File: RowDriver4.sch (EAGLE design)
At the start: 25 parts, among them Q1 DPBT8105, Q2 DPBT8105, Q3 DPBT8105, Q4 DPBT8105

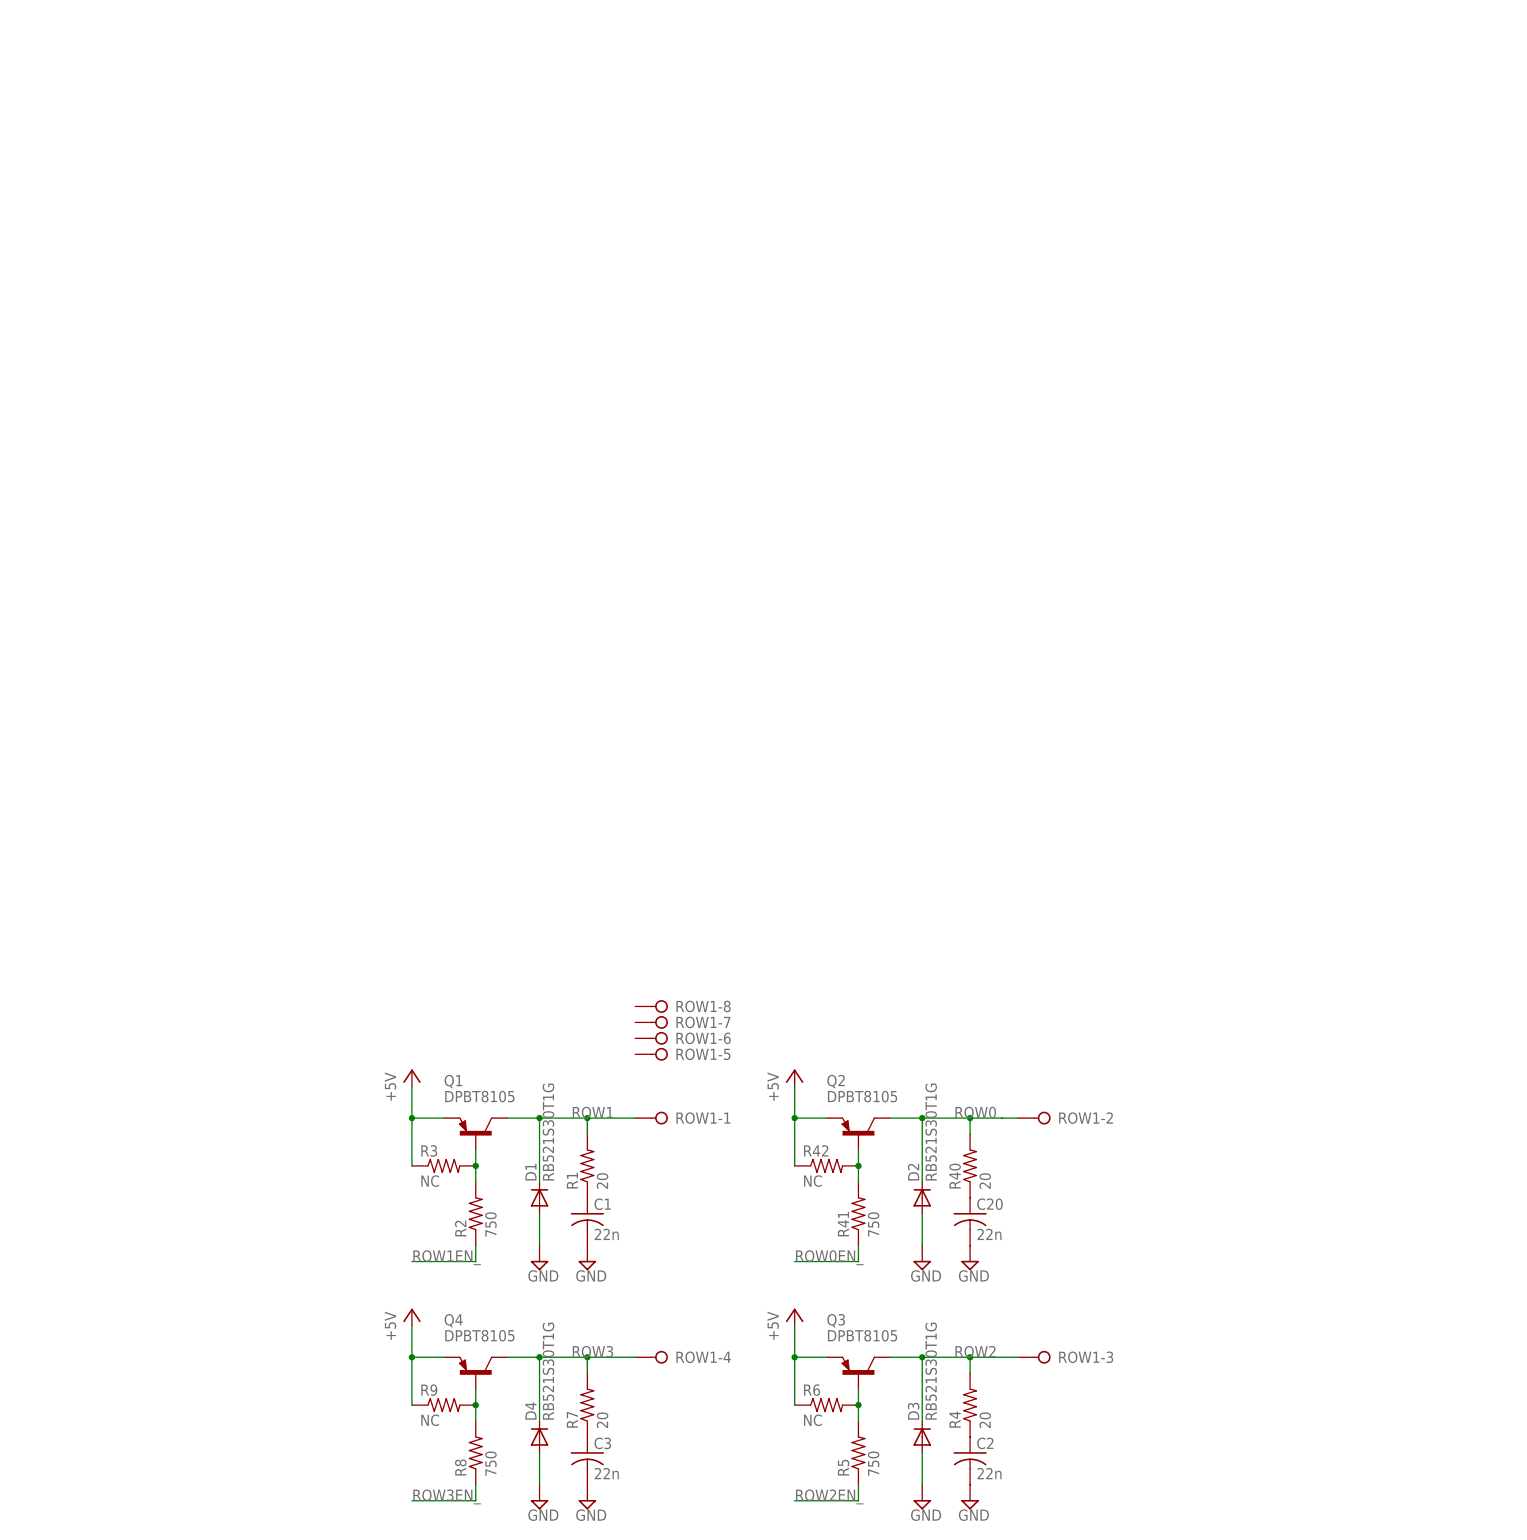
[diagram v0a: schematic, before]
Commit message: Created initial main board. Created layout for row driver, and tiled it. The new board and schematic files for the row driver are intermediate steps.
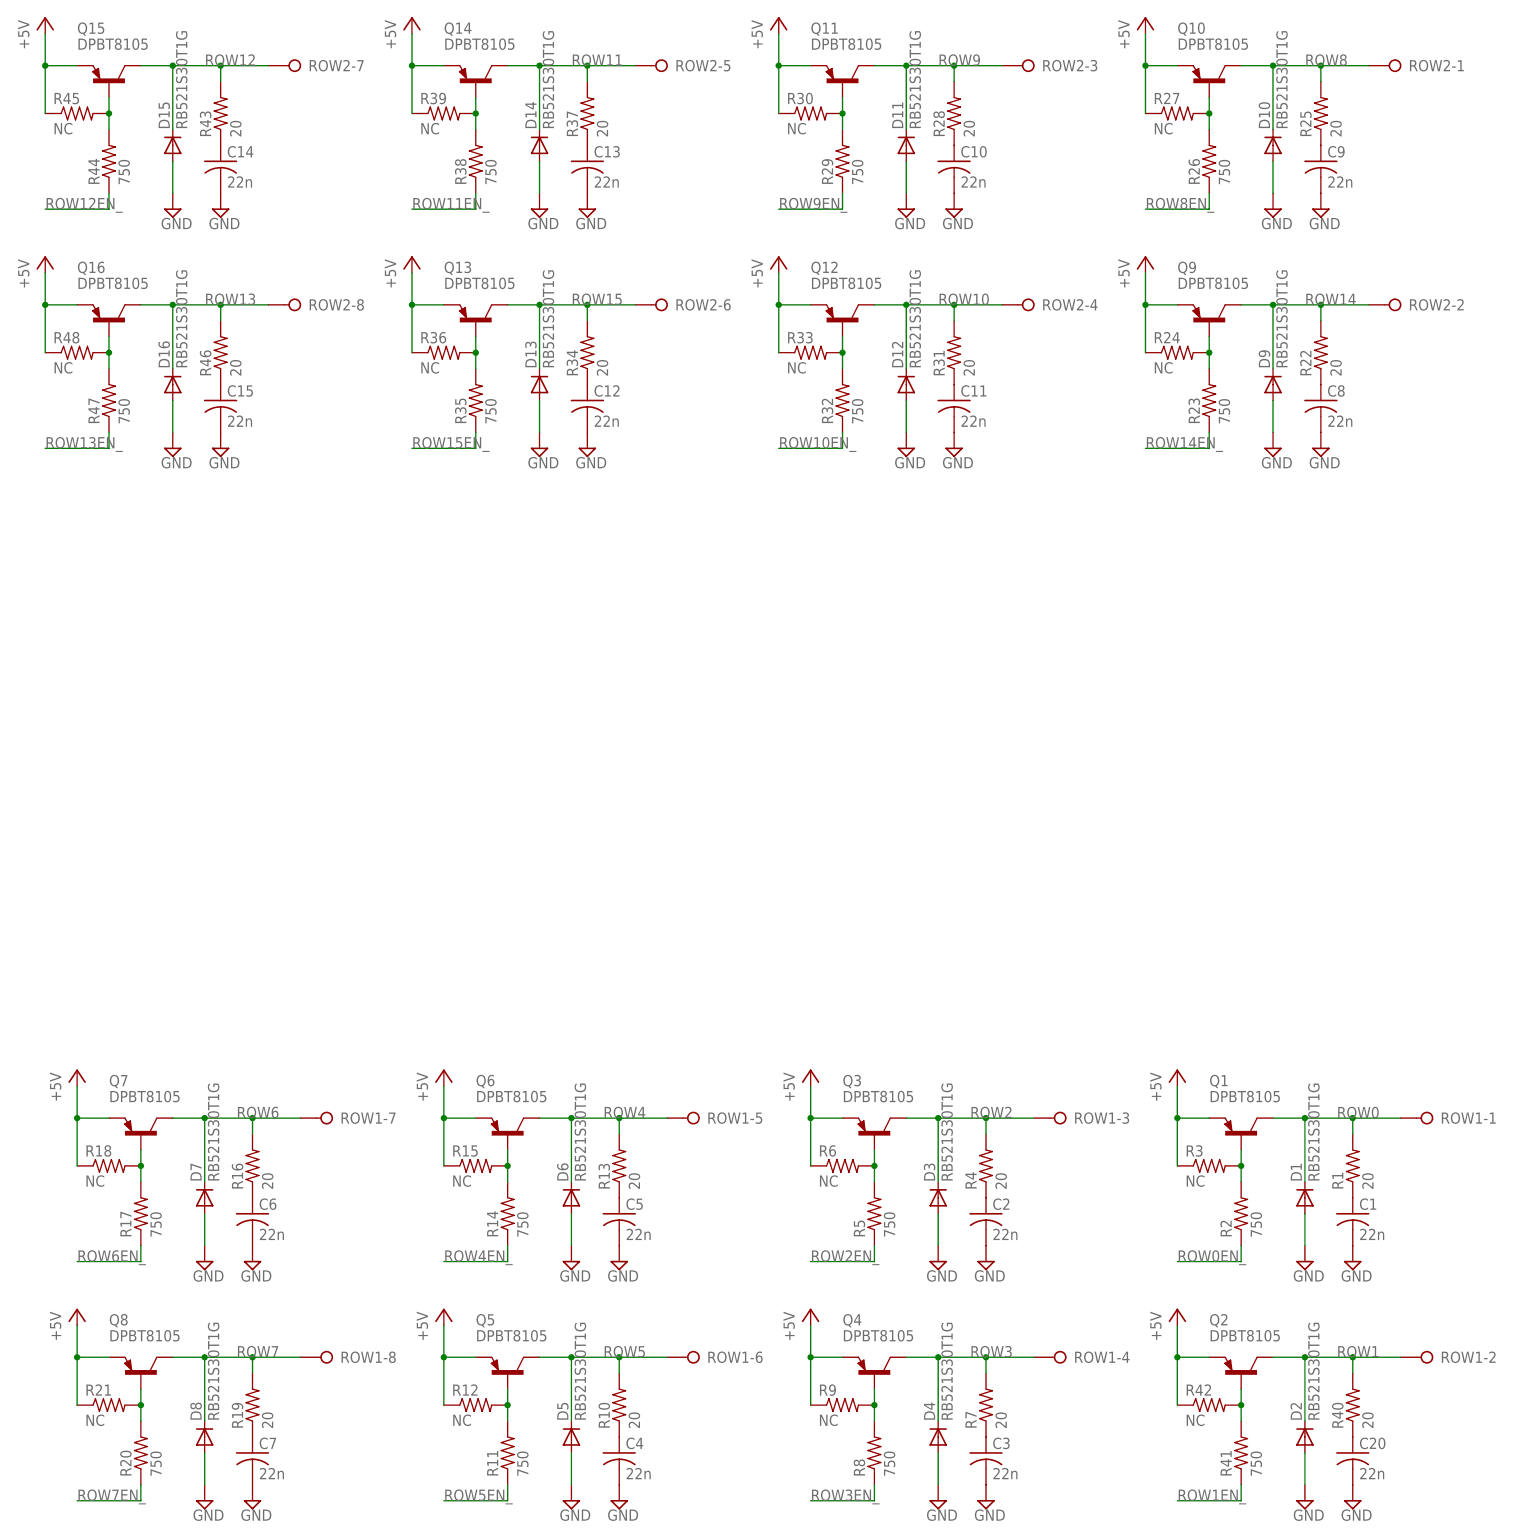
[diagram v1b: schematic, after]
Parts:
- added C10, C11, C12, C13, C14, C15, C4, C5, C6, C7, C8, C9: 22n, resistor:C-USC0603
- added D10, D11, D12, D13, D14, D15, D16, D5, D6, D7, D8, D9: RB521S30T1G, diode:DIODE-SOD523
- added Q10, Q11, Q12, Q13, Q14, Q15, Q16, Q5, Q6, Q7, Q8, Q9: DPBT8105, Parts:DPBT8105
- added R10, R13, R16, R19, R22, R25, R28, R31, R34, R37, R43, R46: 20, resistor:R-US_R0603
- added R11, R14, R17, R20, R23, R26, R29, R32, R35, R38, R44, R47: 750, resistor:R-US_R0603
- added R12, R15, R18, R21, R24, R27, R30, R33, R36, R39, R45, R48: NC, resistor:R-US_R0603
- added ROW2: (no value), Parts:OSTVN08A150
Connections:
- new net N$10: C5.1, R13.1
- new net N$11: Q7.B, R17.2, R18.2
- new net N$12: C6.1, R16.1
- new net N$13: Q8.B, R20.2, R21.2
- new net N$14: C7.1, R19.1
- new net N$15: Q9.B, R23.2, R24.2
- new net N$16: C8.1, R22.1
- new net N$17: Q10.B, R26.2, R27.2
- new net N$18: C9.1, R25.1
- new net N$19: Q11.B, R29.2, R30.2
- new net N$20: C10.1, R28.1
- new net N$21: Q12.B, R32.2, R33.2
- new net N$22: C11.1, R31.1
- new net N$23: Q13.B, R35.2, R36.2
- new net N$24: C12.1, R34.1
- new net N$25: Q14.B, R38.2, R39.2
- new net N$26: C13.1, R37.1
- new net N$27: Q15.B, R44.2, R45.2
- new net N$28: C14.1, R43.1
- new net N$29: Q16.B, R47.2, R48.2
- new net N$30: C15.1, R46.1
- new net N$7: Q5.B, R11.2, R12.2
- new net N$8: C4.1, R10.1
- new net N$9: Q6.B, R14.2, R15.2
- new net ROW10: D12.C, Q12.C, R31.2, ROW2-4.KL
- new net ROW10EN_: R32.1
- new net ROW11: D14.C, Q14.C, R37.2, ROW2-5.KL
- new net ROW11EN_: R38.1
- new net ROW12: D15.C, Q15.C, R43.2, ROW2-7.KL
- new net ROW12EN_: R44.1
- new net ROW13: D16.C, Q16.C, R46.2, ROW2-8.KL
- new net ROW13EN_: R47.1
- new net ROW14: D9.C, Q9.C, R22.2, ROW2-2.KL
- new net ROW14EN_: R23.1
- new net ROW15: D13.C, Q13.C, R34.2, ROW2-6.KL
- new net ROW15EN_: R35.1
- new net ROW4: D6.C, Q6.C, R13.2, ROW1-5.KL
- new net ROW4EN_: R14.1
- new net ROW5: D5.C, Q5.C, R10.2, ROW1-6.KL
- new net ROW5EN_: R11.1
- new net ROW6: D7.C, Q7.C, R16.2, ROW1-7.KL
- new net ROW6EN_: R17.1
- new net ROW7: D8.C, Q8.C, R19.2, ROW1-8.KL
- new net ROW7EN_: R20.1
- new net ROW8: D10.C, Q10.C, R25.2, ROW2-1.KL
- new net ROW8EN_: R26.1
- new net ROW9: D11.C, Q11.C, R28.2, ROW2-3.KL
- new net ROW9EN_: R29.1
- net +5V: now also Q10.E, Q11.E, Q12.E, Q13.E, Q14.E, Q15.E, Q16.E, Q5.E, Q6.E, Q7.E, Q8.E, Q9.E, R12.1, R15.1, R18.1, R21.1, R24.1, R27.1, R30.1, R33.1, R36.1, R39.1, R45.1, R48.1
- net GND: now also C10.2, C11.2, C12.2, C13.2, C14.2, C15.2, C4.2, C5.2, C6.2, C7.2, C8.2, C9.2, D10.A, D11.A, D12.A, D13.A, D14.A, D15.A, D16.A, D5.A, D6.A, D7.A, D8.A, D9.A
- net ROW0: now also D1.C, Q1.C, R1.2, ROW1-1.KL; no longer D2.C, Q2.C, R40.2, ROW1-2.KL
- net ROW0EN_: now also R2.1; no longer R41.1
- net ROW1: now also D2.C, Q2.C, R40.2, ROW1-2.KL; no longer D1.C, Q1.C, R1.2, ROW1-1.KL
- net ROW1EN_: now also R41.1; no longer R2.1
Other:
- moved on the sheet: C1, C2, C20, C3, D1, D2, D3, D4, Q1, Q2, Q3, Q4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

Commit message: Iterated through a few possible board floorplans.  Routing will be incredibly tight, but I thought of a few possibilities that ease those concerns.
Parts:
- added C16, C21, C22, C89, C90, C91, C92, C94, C95, C96, C97, C98: NC, rcl:C-USC0805
- added C17, C18, C19, C26, C27, C28, C29, C31, C33, C93: 0.1uF, rcl:C-USC0805
- added C23: 470pF, rcl:C-USC0805
- added C24, C38: 10uF, rcl:C-USC1206K
- added C25, C30, C32, C36, C39: 1uF, rcl:C-USC0805
- added C34, C35, C37, C40: 100uF, resistor:CPOL-USD
- added C41, C42, C43, C44, C45, C46, C47, C48, C49, C50, C51, C52, C53, C54, C55, C56, C57, C58, C59, C60, C61, C62, C63, C64, C65, C66, C67, C68, C69, C70, C71, C72, C73, C74, C75, C76, C77, C78, C79, C80, C81, C82, C83, C84, C85, C86, C87, C88: 1n, resistor:C-USC0805
- added D17, D18, D19, D20, D21, D22, D23, D24, D25, D26, D27, D28, D29, D30, D31, D32, D33, D34, D35, D36, D37, D38, D39, D40, D41, D42, D43, D44, D45, D46, D47, D48, D49, D50, D51, D52, D53, D54, D55, D56, D57, D58, D59, D60, D61, D62, D63, D64: RB521S30T1G, diode:DIODE-SOD523
- added IC1, IC2: 74HCT138D, Parts:74HCT138D
- added IC3: PIC24FJ32GB004, Parts:PIC24FJ32GB004
- added IC4, IC5: SN74LV4052AD, Parts:SN74LV4052AD
- added IC6: TC1015, Parts:TC1015
- added IC7: NCP1117, Parts:NCP1117
- added J1: PWR, con-jack:DCJ0303
- added JP1: DEBUG, pinhead:PINHD-1X5/90
- added LED0, LED1, LED2, LED3: (no value), Parts:OSTVN12A150
- added Q17: NC, transistor:-NPN-SOT23-EBC
- added R100, R101, R102, R103, R104, R105, R106, R107, R108, R109, R110, R111, R112, R113, R114, R115, R116, R117, R118, R119, R120, R121, R122, R123, R124, R125, R126, R127, R128, R129, R130, R131, R132, R133, R134, R135, R88, R89, R90, R91, R92, R93, R94, R95, R96, R97, R98, R99: 300, resistor:R-US_R0805
- added R49, R50, R51, R52, R53, R54, R57, R58, R59, R60: 4.7k, resistor:R-US_R0805
- added R55, R56: 1.37k 0.5%, resistor:R-US_R0805
- added R61, R62, R63, R64, R65, R66, R67, R68, R69, R70, R71, R72, R73, R74, R75, R76, R77, R78, R79, R80, R81, R82, R83: 390, resistor:R-US_R0805
- added R84: 0, resistor:R-US_R0805
- added R85, R86, R87: NC, resistor:R-US_R0805
- added SG1: NC, buzzer:F/CM04P
- added TCH0, TCH1: (no value), Parts:OSTVN11A150
- added U$1, U$2: TLC5952, Parts:TLC5952
- added X1: MINI-USB-32005-201, Parts:MINI-USB-32005-201
- added XTAL1: NC, crystal:CRYSTALHC49UP
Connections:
- new net +3V3: C17.1, C18.1, C19.1, C24.1, C26.1, C27.1, C30.1, C31.1, C32.1, C33.1, C89.1, C90.1, C91.1, C93.1, C94.1, C95.1, C98.1, IC3.AVDD, IC3.VDD@1, IC3.VDD@2, IC3.VUSB, IC4.VCC, IC5.VCC, IC6.VOUT, JP1.2, R60.2, R85.2, U$1.VCC, U$2.VCC
- new net AMSEL0: IC3.RB8, IC4.A, IC5.A
- new net AMSEL1: IC3.RB9, IC4.B, IC5.B
- new net B0: D19.A, LED0-3.KL, R90.2, U$1.OUTB0
- new net B1: D22.A, LED0-6.KL, R93.2, U$1.OUTB1
- new net B10: D49.A, LED2-9.KL, R120.2, U$2.OUTB2
- new net B11: D52.A, LED2-12.KL, R123.2, U$2.OUTB3
- new net B12: D55.A, LED3-3.KL, R126.2, U$2.OUTB4
- new net B13: D58.A, LED3-6.KL, R129.2, U$2.OUTB5
- new net B14: D61.A, LED3-9.KL, R132.2, U$2.OUTB6
- new net B15: D64.A, LED3-12.KL, R135.2, U$2.OUTB7
- new net B2: D25.A, LED0-9.KL, R96.2, U$1.OUTB2
- new net B3: D28.A, LED0-12.KL, R99.2, U$1.OUTB3
- new net B4: D31.A, LED1-3.KL, R102.2, U$1.OUTB4
- new net B5: D34.A, LED1-6.KL, R105.2, U$1.OUTB5
- new net B6: D37.A, LED1-9.KL, R108.2, U$1.OUTB6
- new net B7: D40.A, LED1-12.KL, R111.2, U$1.OUTB7
- new net B8: D43.A, LED2-3.KL, R114.2, U$2.OUTB0
- new net B9: D46.A, LED2-6.KL, R117.2, U$2.OUTB1
- new net C0_LAT: IC3.RP4, U$1.LAT
- new net C0_SCLK: IC3.RP20, U$1.SCLK
- new net C0_SIN: IC3.RP21, U$1.SIN
- new net C0_SOUT: IC3.RP7, U$1.SOUT
- new net C1_LAT: IC3.RP22, U$2.LAT
- new net C1_SCLK: IC3.RP23, U$2.SCLK
- new net C1_SIN: IC3.RP24, U$2.SIN
- new net C1_SOUT: IC3.RP25, U$2.SOUT
- new net CAIREF: R55.2, U$1.IREF
- new net CAIREF1: R56.2, U$2.IREF
- new net C_BLANK: IC3.RB5, U$1.BLANK, U$2.BLANK
- new net D+: IC3.D+, X1.3
- new net D-: IC3.D-, X1.2
- new net DISVREG: IC3.DISVREG, R59.2
- new net G0: D18.A, LED0-2.KL, R89.2, U$1.OUTG0
- new net G1: D21.A, LED0-5.KL, R92.2, U$1.OUTG1
- new net G10: D48.A, LED2-8.KL, R119.2, U$2.OUTG2
- new net G11: D51.A, LED2-11.KL, R122.2, U$2.OUTG3
- new net G12: D54.A, LED3-2.KL, R125.2, U$2.OUTG4
- new net G13: D57.A, LED3-5.KL, R128.2, U$2.OUTG5
- new net G14: D60.A, LED3-8.KL, R131.2, U$2.OUTG6
- new net G15: D63.A, LED3-11.KL, R134.2, U$2.OUTG7
- new net G2: D24.A, LED0-8.KL, R95.2, U$1.OUTG2
- new net G3: D27.A, LED0-11.KL, R98.2, U$1.OUTG3
- new net G4: D30.A, LED1-2.KL, R101.2, U$1.OUTG4
- new net G5: D33.A, LED1-5.KL, R104.2, U$1.OUTG5
- new net G6: D36.A, LED1-8.KL, R107.2, U$1.OUTG6
- new net G7: D39.A, LED1-11.KL, R110.2, U$1.OUTG7
- new net G8: D42.A, LED2-2.KL, R113.2, U$2.OUTG0
- new net G9: D45.A, LED2-5.KL, R116.2, U$2.OUTG1
- new net MCLR_: IC3.!MCLR, JP1.1, R61.1
- new net N$100: C52.1, R99.1
- new net N$101: C53.1, R100.1
- new net N$102: C54.1, R101.1
- new net N$103: C55.1, R102.1
- new net N$104: C56.1, R103.1
- new net N$105: C57.1, R104.1
- new net N$106: C58.1, R105.1
- new net N$107: C59.1, R106.1
- new net N$108: C60.1, R107.1
- new net N$109: C61.1, R108.1
- new net N$110: C62.1, R109.1
- new net N$111: C63.1, R110.1
- new net N$112: C64.1, R111.1
- new net N$114: C65.1, R112.1
- new net N$116: C66.1, R113.1
- new net N$118: C67.1, R114.1
- new net N$120: C68.1, R115.1
- new net N$122: C69.1, R116.1
- new net N$124: C70.1, R117.1
- new net N$126: C71.1, R118.1
- new net N$128: C72.1, R119.1
- new net N$130: C73.1, R120.1
- new net N$132: C74.1, R121.1
- new net N$134: C75.1, R122.1
- new net N$136: C76.1, R123.1
- new net N$138: C77.1, R124.1
- new net N$140: C78.1, R125.1
- new net N$142: C79.1, R126.1
- new net N$144: C80.1, R127.1
- new net N$146: C81.1, R128.1
- new net N$148: C82.1, R129.1
- new net N$150: C83.1, R130.1
- new net N$152: C84.1, R131.1
- new net N$154: C85.1, R132.1
- new net N$156: C86.1, R133.1
- new net N$158: C87.1, R134.1
- new net N$160: C88.1, R135.1
- new net N$41: IC1.G2A, IC1.G2B, R50.2
- new net N$42: IC4.INH, R51.2
- new net N$43: IC2.G2A, IC2.G2B, R53.2
- new net N$44: IC5.INH, R54.2
- new net N$45: IC3.VBUS, R58.2
- new net N$46: C16.1, R60.1, R61.2
- new net N$47: R62.2, TCH0-1.KL
- new net N$48: R63.2, TCH0-2.KL
- new net N$65: R64.2, TCH0-3.KL
- new net N$66: R65.2, TCH0-4.KL
- new net N$67: R66.2, TCH0-5.KL
- new net N$68: R67.2, TCH0-6.KL
- new net N$69: R68.2, TCH0-7.KL
- new net N$70: R69.2, TCH0-8.KL
- new net N$71: R70.2, TCH0-9.KL
- new net N$72: R71.2, TCH0-10.KL
- new net N$73: R72.2, TCH0-11.KL
- new net N$74: R74.2, TCH1-2.KL
- new net N$75: R76.2, TCH1-4.KL
- new net N$76: R78.2, TCH1-6.KL
- new net N$77: R80.2, TCH1-8.KL
- new net N$78: R82.2, TCH1-10.KL
- new net N$79: R73.2, TCH1-1.KL
- new net N$80: R75.2, TCH1-3.KL
- new net N$81: R77.2, TCH1-5.KL
- new net N$82: R79.2, TCH1-7.KL
- new net N$83: R81.2, TCH1-9.KL
- new net N$84: R83.2, TCH1-11.KL
- new net N$85: C23.1, IC6.BYPASS
- new net N$86: R85.1, R86.2
- new net N$87: Q17.B, R87.2
- new net N$88: Q17.C, SG1.2
- new net N$89: C41.1, R88.1
- new net N$90: C42.1, R89.1
- new net N$91: C43.1, R90.1
- new net N$92: C44.1, R91.1
- new net N$93: C45.1, R92.1
- new net N$94: C46.1, R93.1
- new net N$95: C47.1, R94.1
- new net N$96: C48.1, R95.1
- new net N$97: C49.1, R96.1
- new net N$98: C50.1, R97.1
- new net N$99: C51.1, R98.1
- new net OSCI: C22.1, IC3.OSCI, XTAL1.1
- new net OSCO: C21.1, IC3.OSCO, XTAL1.2
- new net PGEC: IC3.PGEC1, JP1.5
- new net PGED: IC3.PGED1, JP1.4
- new net R0: D17.A, LED0-1.KL, R88.2, U$1.OUTR0
- new net R1: D20.A, LED0-4.KL, R91.2, U$1.OUTR1
- new net R10: D47.A, LED2-7.KL, R118.2, U$2.OUTR2
- new net R11: D50.A, LED2-10.KL, R121.2, U$2.OUTR3
- new net R12: D53.A, LED3-1.KL, R124.2, U$2.OUTR4
- new net R13: D56.A, LED3-4.KL, R127.2, U$2.OUTR5
- new net R14: D59.A, LED3-7.KL, R130.2, U$2.OUTR6
- new net R15: D62.A, LED3-10.KL, R133.2, U$2.OUTR7
- new net R2: D23.A, LED0-7.KL, R94.2, U$1.OUTR2
- new net R3: D26.A, LED0-10.KL, R97.2, U$1.OUTR3
- new net R4: D29.A, LED1-1.KL, R100.2, U$1.OUTR4
- new net R5: D32.A, LED1-4.KL, R103.2, U$1.OUTR5
- new net R6: D35.A, LED1-7.KL, R106.2, U$1.OUTR6
- new net R7: D38.A, LED1-10.KL, R109.2, U$1.OUTR7
- new net R8: D41.A, LED2-1.KL, R112.2, U$2.OUTR0
- new net R9: D44.A, LED2-4.KL, R115.2, U$2.OUTR1
- new net RAEN: IC1.G1, IC3.RA10, R49.2
- new net RBEN: IC2.G1, IC3.RA4, R52.2
- new net RSEL0: IC1.A, IC2.A, IC3.RA7
- new net RSEL1: IC1.B, IC2.B, IC3.RA8
- new net RSEL2: IC1.C, IC2.C, IC3.RA9
- new net TMUX0: IC3.AN11, IC4.Y
- new net TMUX1: IC3.AN10, IC4.X
- new net TMUX2: IC3.AN5, IC5.Y
- new net TMUX3: IC3.AN6, IC5.X
- new net TOUCH0: IC4.Y0, R62.1
- new net TOUCH1: IC4.Y1, R63.1
- new net TOUCH10: IC3.AN4, R72.1
- new net TOUCH11: IC5.Y0, R73.1
- new net TOUCH12: IC5.Y1, R74.1
- new net TOUCH13: IC5.Y2, R75.1
- new net TOUCH14: IC5.Y3, R76.1
- new net TOUCH15: IC5.X0, R77.1
- new net TOUCH16: IC5.X1, R78.1
- new net TOUCH17: IC5.X2, R79.1
- new net TOUCH18: IC5.X3, R80.1
- new net TOUCH19: IC3.AN7, R81.1
- new net TOUCH2: IC4.Y2, R64.1
- new net TOUCH20: IC3.AN8, R82.1
- new net TOUCH21: IC3.AN12, R83.1
- new net TOUCH3: IC4.Y3, R65.1
- new net TOUCH4: IC4.X0, R66.1
- new net TOUCH5: IC4.X1, R67.1
- new net TOUCH6: IC4.X2, R68.1
- new net TOUCH7: IC4.X3, R69.1
- new net TOUCH8: IC3.AN9, R70.1
- new net TOUCH9: IC3.AN1, R71.1
- new net V+: C35.+, IC7G$1.IN, J1.1, R84.1
- new net VBUS: R57.2, R58.1, X1.1
- new net VDDCORE: C38.1, C92.1, IC3.VDDCORE
- new net VREF+: IC3.VREF+, R87.1
- net +5V: now also C25.1, C28.1, C29.1, C34.+, C36.1, C37.+, C39.1, C40.+, C96.1, C97.1, D17.C, D18.C, D19.C, D20.C, D21.C, D22.C, D23.C, D24.C, D25.C, D26.C, D27.C, D28.C, D29.C, D30.C, D31.C, D32.C, D33.C, D34.C, D35.C, D36.C, D37.C, D38.C, D39.C, D40.C, D41.C, D42.C, D43.C, D44.C, D45.C, D46.C, D47.C, D48.C, D49.C, D50.C, D51.C, D52.C, D53.C, D54.C, D55.C, D56.C, D57.C, D58.C, D59.C, D60.C, D61.C, D62.C, D63.C, D64.C, IC1.VCC, IC2.VCC, IC6.SHDN_, IC6.VIN, IC7G$1.OUT, R84.2, SG1.1
- net GND: now also C16.2, C17.2, C18.2, C19.2, C21.2, C22.2, C23.2, C24.2, C25.2, C26.2, C27.2, C28.2, C29.2, C30.2, C31.2, C32.2, C33.2, C34.-, C35.-, C36.2, C37.-, C38.2, C39.2, C40.-, C41.2, C42.2, C43.2, C44.2, C45.2, C46.2, C47.2, C48.2, C49.2, C50.2, C51.2, C52.2, C53.2, C54.2, C55.2, C56.2, C57.2, C58.2, C59.2, C60.2, C61.2, C62.2, C63.2, C64.2, C65.2, C66.2, C67.2, C68.2, C69.2, C70.2, C71.2, C72.2, C73.2, C74.2, C75.2, C76.2, C77.2, C78.2, C79.2, C80.2, C81.2, C82.2, C83.2, C84.2, C85.2, C86.2, C87.2, C88.2, C89.2, C90.2, C91.2, C92.2, C93.2, C94.2, C95.2, C96.2, C97.2, C98.2, IC1.GND, IC2.GND, IC3.AVSS, IC3.VSS@1, IC3.VSS@2, IC4.GND, IC5.GND, IC6.GND, IC7G$1.GND, J1.2, J1.3, JP1.3, Q17.E, R49.1, R50.1, R51.1, R52.1, R53.1, R54.1, R55.1, R56.1, R57.1, R59.1, R86.1, U$1.EPAD, U$1.GND, U$2.EPAD, U$2.GND, X1.5
- net ROW0EN_: now also IC1.Y0
- net ROW10EN_: now also IC2.Y2
- net ROW11EN_: now also IC2.Y3
- net ROW12EN_: now also IC2.Y4
- net ROW13EN_: now also IC2.Y5
- net ROW14EN_: now also IC2.Y6
- net ROW15EN_: now also IC2.Y7
- net ROW1EN_: now also IC1.Y1
- net ROW2EN_: now also IC1.Y2
- net ROW3EN_: now also IC1.Y3
- net ROW4EN_: now also IC1.Y4
- net ROW5EN_: now also IC1.Y5
- net ROW6EN_: now also IC1.Y6
- net ROW7EN_: now also IC1.Y7
- net ROW8EN_: now also IC2.Y0
- net ROW9EN_: now also IC2.Y1
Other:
- moved on the sheet: C1, C10, C11, C12, C13, C14, C15, C2, C20, C3, C4, C5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
